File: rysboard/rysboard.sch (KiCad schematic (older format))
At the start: 8 parts, among them J1 RPi4, J17 Conn_01x03

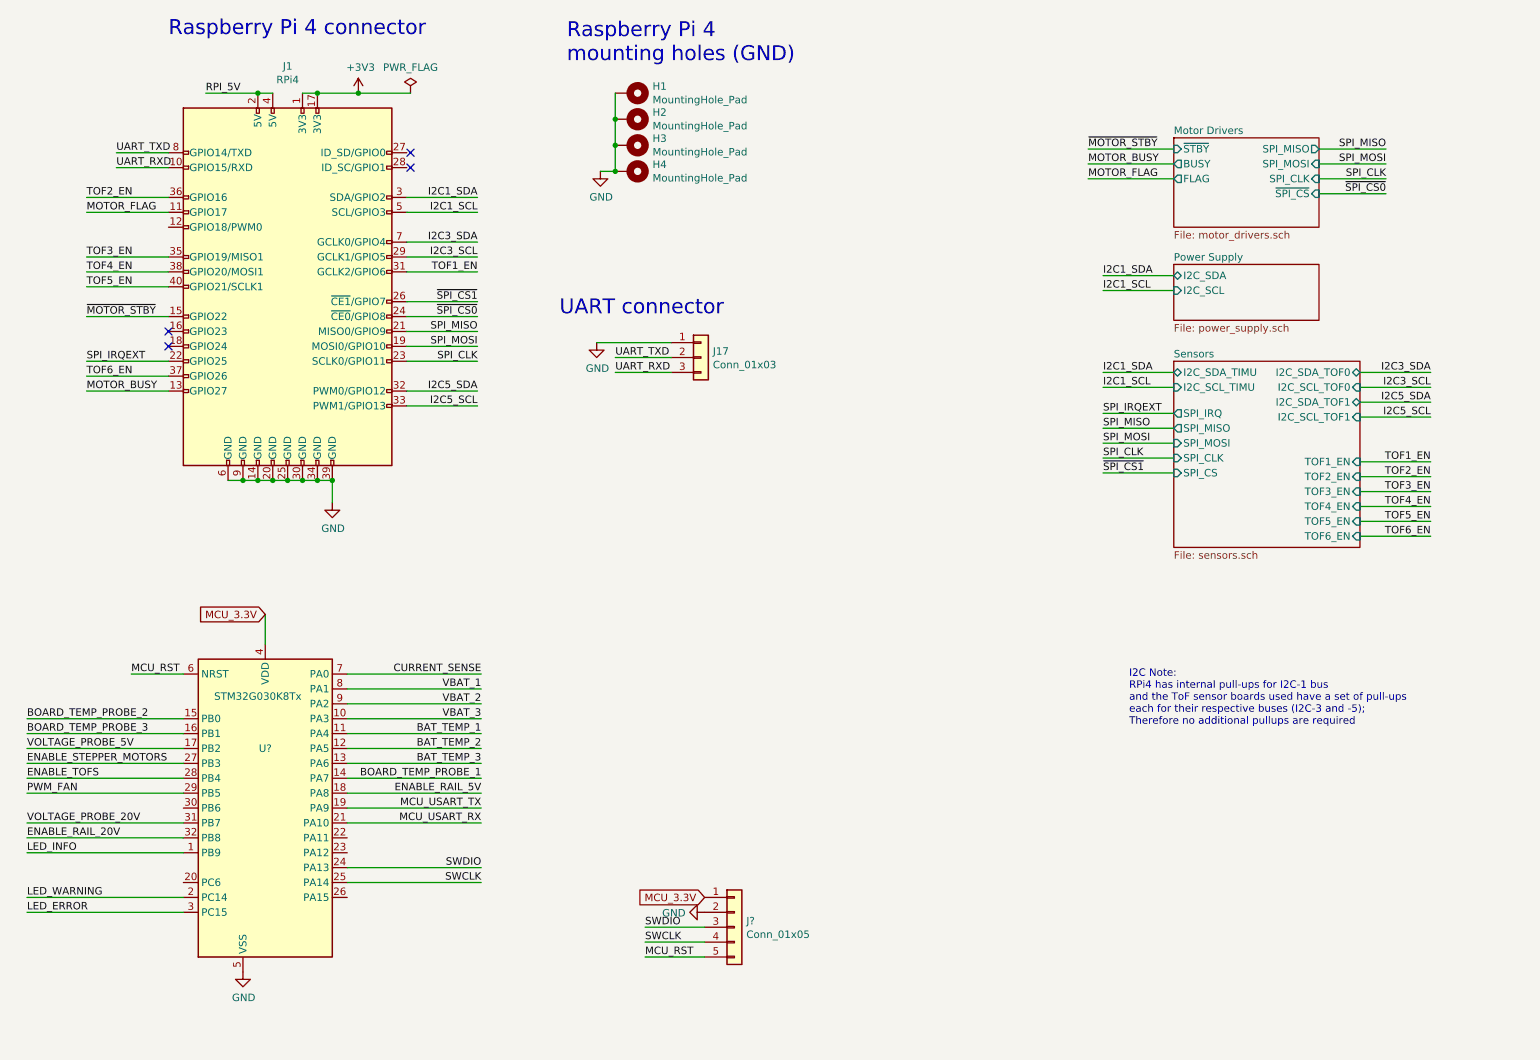
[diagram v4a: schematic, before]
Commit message: DMP3036SSD footprint added
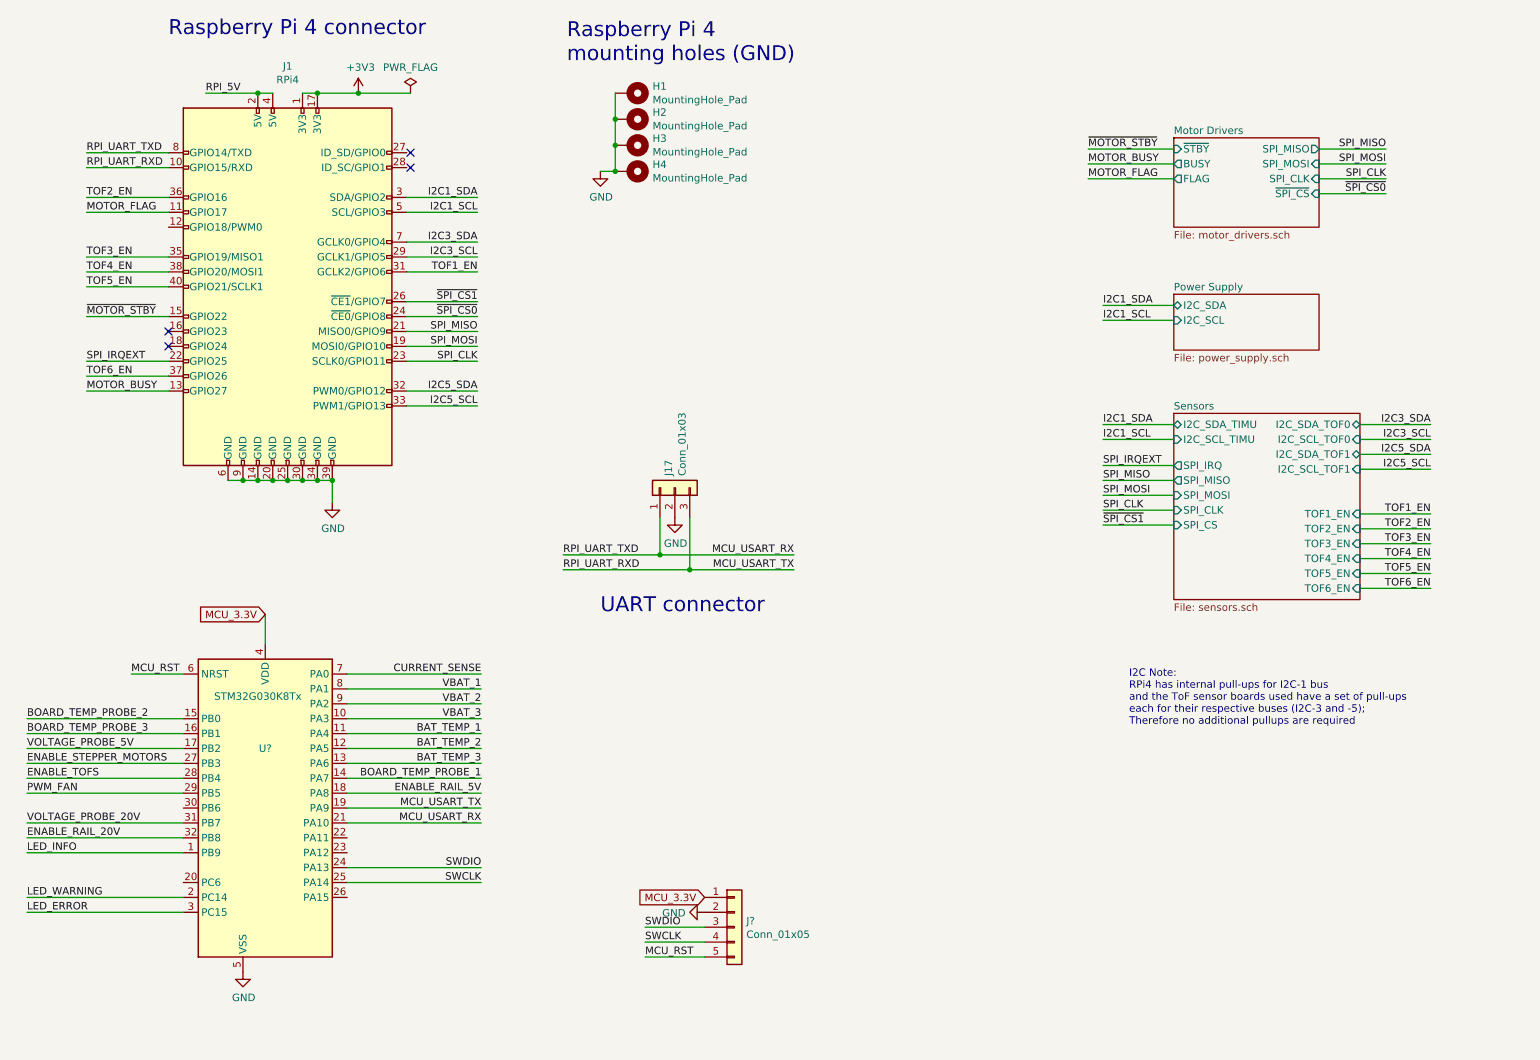
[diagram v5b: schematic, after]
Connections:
- net UART_RXD is gone; now on net MCU_USART_TX: J1.10 (GPIO15/RXD), J17.3 (Pin_3)
- net GND: now also J17.2 (Pin_2); no longer J17.1 (Pin_1)
- net MCU_USART_RX: now also J1.8 (GPIO14/TXD), J17.1 (Pin_1)
- removed net UART_TXD: J1.8 (GPIO14/TXD), J17.2 (Pin_2)
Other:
- moved on the sheet: J17
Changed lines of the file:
@@
 Raspberry Pi 4 connector
 $Sheet
-S 8250 2350 975  375
+S 8250 2550 975  375
 U 5E8FCBC6
 F0 "Power Supply" 50
 F1 "power_supply.sch" 50
-F2 "I2C_SDA" B L 8250 2425 50
-F3 "I2C_SCL" I L 8250 2525 50
+F2 "I2C_SDA" B L 8250 2625 50
+F3 "I2C_SCL" I L 8250 2725 50
 $EndSheet
 Text Label 3575 2700 2    50   ~ 0
@@
 Text Label 9675 1875 2    50   ~ 0
 ~SPI_CS0
-Text Label 7775 3450 0    50   ~ 0
+Text Label 7775 3800 0    50   ~ 0
 SPI_MISO
-Text Label 7775 3550 0    50   ~ 0
+Text Label 7775 3900 0    50   ~ 0
 SPI_MOSI
-Text Label 7775 3650 0    50   ~ 0
+Text Label 7775 4000 0    50   ~ 0
 SPI_CLK
-Text Label 7775 3750 0    50   ~ 0
+Text Label 7775 4100 0    50   ~ 0
 ~SPI_CS1
 Wire Wire Line
-	8250 3450 7775 3450
-Wire Wire Line
-	7775 3550 8250 3550
-Wire Wire Line
-	8250 3650 7775 3650
-Wire Wire Line
-	7775 3750 8250 3750
-Wire Wire Line
-	9500 3675 9975 3675
-Wire Wire Line
-	9500 3775 9975 3775
-Text Label 9975 3675 2    50   ~ 0
+	8250 3800 7775 3800
+Wire Wire Line
+	7775 3900 8250 3900
+Wire Wire Line
+	8250 4000 7775 4000
+Wire Wire Line
+	7775 4100 8250 4100
+Wire Wire Line
+	9500 4025 9975 4025
+Wire Wire Line
+	9500 4125 9975 4125
+Text Label 9975 4025 2    50   ~ 0
 TOF1_EN
-Text Label 9975 3775 2    50   ~ 0
+Text Label 9975 4125 2    50   ~ 0
 TOF2_EN
-Text Label 7775 3350 0    50   ~ 0
+Text Label 7775 3700 0    50   ~ 0
 SPI_IRQEXT
 Wire Wire Line
-	9500 3875 9975 3875
-Text Label 9975 3875 2    50   ~ 0
+	9500 4225 9975 4225
+Text Label 9975 4225 2    50   ~ 0
 TOF3_EN
-Text Label 9975 3975 2    50   ~ 0
+Text Label 9975 4325 2    50   ~ 0
 TOF4_EN
-Text Label 9975 4075 2    50   ~ 0
+Text Label 9975 4425 2    50   ~ 0
 TOF5_EN
-Text Label 9975 4175 2    50   ~ 0
+Text Label 9975 4525 2    50   ~ 0
 TOF6_EN
 Wire Wire Line
-	9500 3975 9975 3975
-Wire Wire Line
-	9500 4075 9975 4075
-Wire Wire Line
-	9500 4175 9975 4175
+	9500 4325 9975 4325
+Wire Wire Line
+	9500 4425 9975 4425
+Wire Wire Line
+	9500 4525 9975 4525
 NoConn ~ 3125 1700
 NoConn ~ 3125 1600
@@
 I2C5_SCL
 Wire Wire Line
-	7775 3350 8250 3350
+	7775 3700 8250 3700
 $Sheet
-S 8250 3000 1250 1250
+S 8250 3350 1250 1250
 U 5EA6D11C
 F0 "Sensors" 50
 F1 "sensors.sch" 50
-F2 "TOF6_EN" I R 9500 4175 50
-F3 "TOF5_EN" I R 9500 4075 50
-F4 "TOF4_EN" I R 9500 3975 50
-F5 "TOF2_EN" I R 9500 3775 50
-F6 "TOF1_EN" I R 9500 3675 50
-F7 "TOF3_EN" I R 9500 3875 50
-F8 "SPI_MOSI" I L 8250 3550 50
-F9 "SPI_MISO" O L 8250 3450 50
-F10 "SPI_CLK" I L 8250 3650 50
-F11 "SPI_CS" I L 8250 3750 50
-F12 "SPI_IRQ" O L 8250 3350 50
-F13 "I2C_SCL_TOF0" I R 9500 3175 50
-F14 "I2C_SDA_TOF0" B R 9500 3075 50
-F15 "I2C_SCL_TIMU" I L 8250 3175 50
-F16 "I2C_SDA_TIMU" B L 8250 3075 50
-F17 "I2C_SCL_TOF1" I R 9500 3375 50
-F18 "I2C_SDA_TOF1" B R 9500 3275 50
+F2 "TOF6_EN" I R 9500 4525 50
+F3 "TOF5_EN" I R 9500 4425 50
+F4 "TOF4_EN" I R 9500 4325 50
+F5 "TOF2_EN" I R 9500 4125 50
+F6 "TOF1_EN" I R 9500 4025 50
+F7 "TOF3_EN" I R 9500 4225 50
+F8 "SPI_MOSI" I L 8250 3900 50
+F9 "SPI_MISO" O L 8250 3800 50
+F10 "SPI_CLK" I L 8250 4000 50
+F11 "SPI_CS" I L 8250 4100 50
+F12 "SPI_IRQ" O L 8250 3700 50
+F13 "I2C_SCL_TOF0" I R 9500 3525 50
+F14 "I2C_SDA_TOF0" B R 9500 3425 50
+F15 "I2C_SCL_TIMU" I L 8250 3525 50
+F16 "I2C_SDA_TIMU" B L 8250 3425 50
+F17 "I2C_SCL_TOF1" I R 9500 3725 50
+F18 "I2C_SDA_TOF1" B R 9500 3625 50
 $EndSheet
 $Comp
 L Connector_Generic:Conn_01x03 J17
 U 1 1 5EA0F66D
-P 5075 2975
-F 0 "J17" H 5155 3017 50  0000 L CNN
-F 1 "Conn_01x03" H 5155 2926 50  0000 L CNN
-F 2 "Connector_PinHeader_2.54mm:PinHeader_1x03_P2.54mm_Vertical" H 5075 2975 50  0001 C CNN
-F 3 "~" H 5075 2975 50  0001 C CNN
-	1    5075 2975
-	1    0    0    -1
-$EndComp
-$Comp
-L power:GND #PWR0101
-U 1 1 5EA0FF92
-P 4375 2875
-F 0 "#PWR0101" H 4375 2625 50  0001 C CNN
-F 1 "GND" H 4380 2702 50  0000 C CNN
-F 2 "" H 4375 2875 50  0001 C CNN
-F 3 "" H 4375 2875 50  0001 C CNN
-	1    4375 2875
-	1    0    0    -1
-$EndComp
-Wire Wire Line
-	4875 2875 4375 2875
-Wire Wire Line
-	4875 2975 4500 2975
-Wire Wire Line
-	4875 3075 4500 3075
-Text Label 4500 2975 0    50   ~ 0
-UART_TXD
-Text Label 4500 3075 0    50   ~ 0
-UART_RXD
-Text Label 1150 1600 0    50   ~ 0
-UART_TXD
-Text Label 1150 1700 0    50   ~ 0
-UART_RXD
-Wire Wire Line
-	9500 3075 9975 3075
-Wire Wire Line
-	9500 3175 9975 3175
-Wire Wire Line
-	9500 3375 9975 3375
-Wire Wire Line
-	9500 3275 9975 3275
-Wire Wire Line
-	7775 3075 8250 3075
-Wire Wire Line
-	7775 3175 8250 3175
-Wire Wire Line
-	7775 2425 8250 2425
-Wire Wire Line
-	7775 2525 8250 2525
-Text Label 7775 2425 0    50   ~ 0
+P 4900 3850
+F 0 "J17" H 4980 3892 50  0000 L CNN
+F 1 "Conn_01x03" H 4980 3801 50  0000 L CNN
+F 2 "Connector_PinHeader_2.54mm:PinHeader_1x03_P2.54mm_Vertical" H 4900 3850 50  0001 C CNN
+F 3 "~" H 4900 3850 50  0001 C CNN
+	1    4900 3850
+	0    -1   -1   0
+$EndComp
+Text Label 4150 4300 0    50   ~ 0
+RPI_UART_TXD
+Text Label 4150 4400 0    50   ~ 0
+RPI_UART_RXD
+Text Label 950  1600 0    50   ~ 0
+RPI_UART_TXD
+Text Label 950  1700 0    50   ~ 0
+RPI_UART_RXD
+Wire Wire Line
+	9500 3425 9975 3425
+Wire Wire Line
+	9500 3525 9975 3525
+Wire Wire Line
+	9500 3725 9975 3725
+Wire Wire Line
+	9500 3625 9975 3625
+Wire Wire Line
+	7775 3425 8250 3425
+Wire Wire Line
+	7775 3525 8250 3525
+Wire Wire Line
+	7775 2625 8250 2625
+Wire Wire Line
+	7775 2725 8250 2725
+Text Label 7775 2625 0    50   ~ 0
 I2C1_SDA
-Text Label 7775 2525 0    50   ~ 0
+Text Label 7775 2725 0    50   ~ 0
 I2C1_SCL
-Text Label 7775 3075 0    50   ~ 0
+Text Label 7775 3425 0    50   ~ 0
 I2C1_SDA
-Text Label 7775 3175 0    50   ~ 0
+Text Label 7775 3525 0    50   ~ 0
 I2C1_SCL
-Text Label 9975 3075 2    50   ~ 0
+Text Label 9975 3425 2    50   ~ 0
 I2C3_SDA
-Text Label 9975 3175 2    50   ~ 0
+Text Label 9975 3525 2    50   ~ 0
 I2C3_SCL
-Text Label 9975 3275 2    50   ~ 0
+Text Label 9975 3625 2    50   ~ 0
 I2C5_SDA
-Text Label 9975 3375 2    50   ~ 0
+Text Label 9975 3725 2    50   ~ 0
 I2C5_SCL
 Text Label 3575 2400 2    50   ~ 0
@@
 Text Label 950  3100 0    50   ~ 0
 TOF6_EN
-Text Notes 4125 2700 0    100  ~ 0
+Text Notes 4400 4700 0    100  ~ 0
 UART connector
 Text Label 950  3000 0    50   ~ 0
@@
 RPI_5V
 Wire Wire Line
-	1500 1600 1150 1600
-Wire Wire Line
 	1500 2500 950  2500
 Wire Wire Line
@@
 Wire Wire Line
 	1500 2000 950  2000
-Wire Wire Line
-	1500 1700 1150 1700
 $Comp
 L Connector:Raspberry_Pi_2_3 J1
@@
 Text GLabel 5100 6600 0    50   Input ~ 0
 MCU_3.3V
+Wire Wire Line
+	950  1700 1500 1700
+Wire Wire Line
+	950  1600 1500 1600
+$Comp
+L power:GND #PWR?
+U 1 1 6046B140
+P 4900 4050
+F 0 "#PWR?" H 4900 3800 50  0001 C CNN
+F 1 "GND" H 4905 3877 50  0000 C CNN
+F 2 "" H 4900 4050 50  0001 C CNN
+F 3 "" H 4900 4050 50  0001 C CNN
+	1    4900 4050
+	1    0    0    -1
+$EndComp
+Text Label 5700 4300 2    50   ~ 0
+MCU_USART_RX
+Text Label 5700 4400 2    50   ~ 0
+MCU_USART_TX
+Wire Wire Line
+	4800 4300 4800 4050
+Wire Wire Line
+	5000 4400 5000 4050
+Wire Wire Line
+	4800 4300 5700 4300
+Wire Wire Line
+	5000 4400 5700 4400
+Wire Wire Line
+	4150 4300 4800 4300
+Connection ~ 4800 4300
+Wire Wire Line
+	4150 4400 5000 4400
+Connection ~ 5000 4400
 $EndSCHEMATC
